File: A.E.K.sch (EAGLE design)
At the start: 7 parts

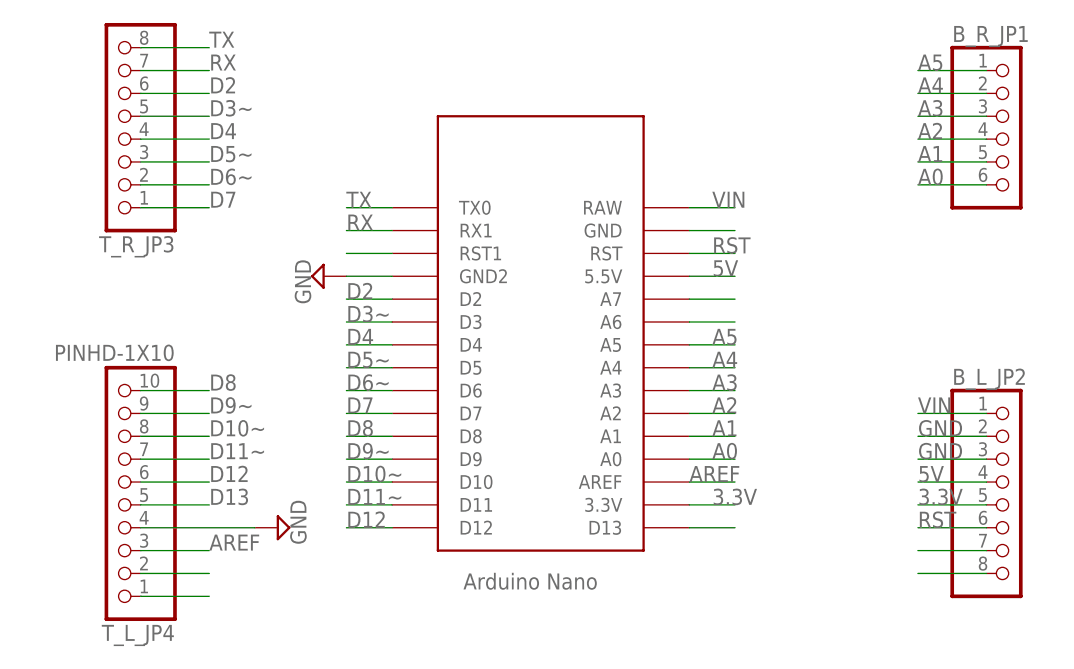
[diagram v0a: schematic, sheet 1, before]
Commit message: schemetics change
remove unroute pin
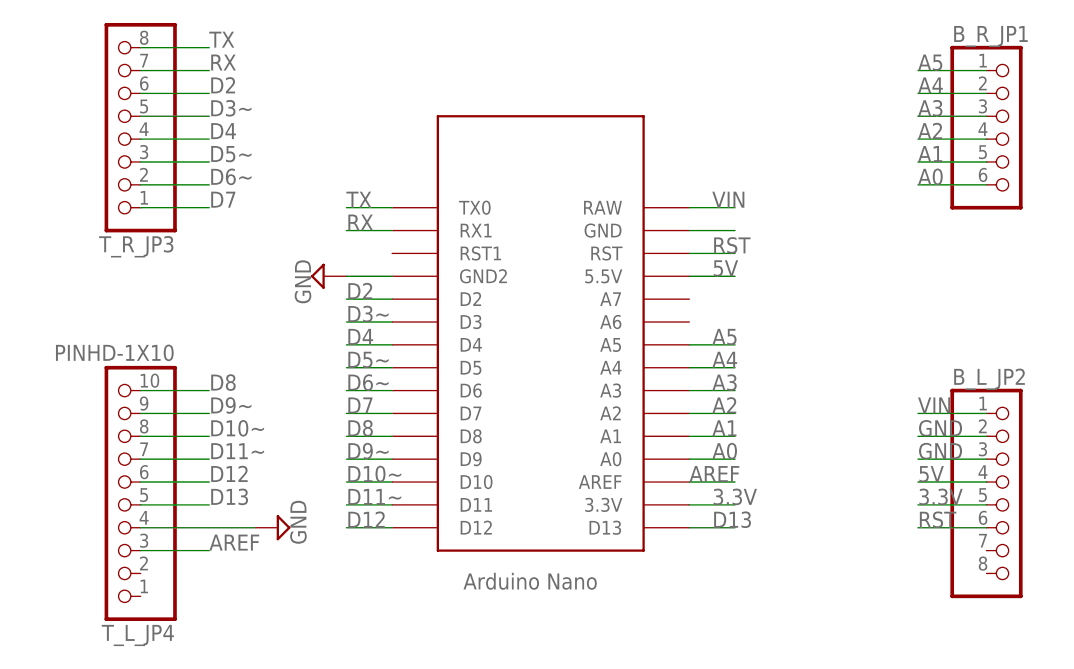
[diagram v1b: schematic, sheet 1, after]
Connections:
- removed net IOREF: B_L_JP2.7
- removed net N$23: B_L_JP2.8
- removed net N$24: U$1.RST1
- removed net N$40: U$1.A7
- removed net N$41: U$1.A6
- removed net N$50: U$1.D13
- removed net SCL: T_L_JP4.1
- removed net SDA: T_L_JP4.2
- net D13: now also U$1.D13
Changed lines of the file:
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@@
 <label x="48.26" y="30.48" size="1.778" layer="95"/>
+</segment>
+<segment>
+<pinref part="U$1" gate="G$1" pin="D13"/>
+<wire x1="101.6" y1="27.94" x2="106.68" y2="27.94" width="0.1524" layer="91"/>
+<label x="104.14" y="27.94" size="1.778" layer="95"/>
 </segment>
 </net>
@@
 </segment>
 </net>
-<net name="SDA" class="0">
-<segment>
-<pinref part="T_L_JP4" gate="G$1" pin="2"/>
-<wire x1="40.64" y1="22.86" x2="48.26" y2="22.86" width="0.1524" layer="91"/>
-</segment>
-</net>
-<net name="SCL" class="0">
-<segment>
-<pinref part="T_L_JP4" gate="G$1" pin="1"/>
-<wire x1="40.64" y1="20.32" x2="48.26" y2="20.32" width="0.1524" layer="91"/>
-</segment>
-</net>
 <net name="3.3V" class="0">
 <segment>
@@
 </segment>
 </net>
-<net name="IOREF" class="0">
-<segment>
-<pinref part="B_L_JP2" gate="G$1" pin="7"/>
-<wire x1="134.62" y1="25.4" x2="127" y2="25.4" width="0.1524" layer="91"/>
-</segment>
-</net>
-<net name="N$23" class="0">
-<segment>
-<pinref part="B_L_JP2" gate="G$1" pin="8"/>
-<wire x1="134.62" y1="22.86" x2="127" y2="22.86" width="0.1524" layer="91"/>
-</segment>
-</net>
-<net name="N$24" class="0">
-<segment>
-<pinref part="U$1" gate="G$1" pin="RST1"/>
-<wire x1="68.58" y1="58.42" x2="63.5" y2="58.42" width="0.1524" layer="91"/>
-</segment>
-</net>
 <net name="D8" class="0">
 <segment>
@@
 <wire x1="134.62" y1="33.02" x2="127" y2="33.02" width="0.1524" layer="91"/>
 <label x="127" y="33.02" size="1.778" layer="95"/>
-</segment>
-</net>
-<net name="N$40" class="0">
-<segment>
-<pinref part="U$1" gate="G$1" pin="A7"/>
-<wire x1="101.6" y1="53.34" x2="106.68" y2="53.34" width="0.1524" layer="91"/>
-</segment>
-</net>
-<net name="N$41" class="0">
-<segment>
-<pinref part="U$1" gate="G$1" pin="A6"/>
-<wire x1="101.6" y1="50.8" x2="106.68" y2="50.8" width="0.1524" layer="91"/>
-</segment>
-</net>
-<net name="N$50" class="0">
-<segment>
-<pinref part="U$1" gate="G$1" pin="D13"/>
-<wire x1="101.6" y1="27.94" x2="106.68" y2="27.94" width="0.1524" layer="91"/>
 </segment>
 </net>
@@
 </sheet>
 </sheets>
-<errors>
-</errors>
 </schematic>
 </drawing>
